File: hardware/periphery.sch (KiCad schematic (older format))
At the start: 32 parts, among them J11 Micro_SD_Card_Ebay, J2 UART0, J8 HR911105_RJ45, Y1 24MHz, Y2 32768

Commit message: Some routing done
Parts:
- removed R37: 2.2, Resistor_SMD:R_0805_2012Metric, symbol Device:R
- removed U? (x2): TLV62568DDC or AP3410/SY8008, Package_TO_SOT_SMD:SOT-23-6, symbol Regulator_Switching:TLV62568DDC
- added C47: 1u, Capacitor_SMD:C_0603_1608Metric, symbol Device:C
- added D1, D2, D3: LED, LED_SMD:LED_0603_1608Metric, symbol Device:LED
- added J1: JAE_SIM_Card_SF72S006, Connector_JAE:JAE_SIM_Card_SF72S006, symbol Connector:JAE_SIM_Card_SF72S006
- added R23: 0R, Resistor_SMD:R_0603_1608Metric, symbol Device:R
- added R26: 10k, Resistor_SMD:R_0603_1608Metric, symbol Device:R
- added R27, R28, R29: 200R, Resistor_SMD:R_0603_1608Metric, symbol Device:R
- C35: value 10u -> 100n; footprint Capacitor_SMD:C_1206_3216Metric -> Capacitor_SMD:C_0603_1608Metric
- J3: renamed from J?; footprint (none) -> Connector_PCBEdge:BUS_PCI_Express_Mini_Full
- gave numbers to parts that had none: 1
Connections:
- net labels added: +1V5, SPI_CS, SPI_MISO, SPI_MOSI, SPI_SCK, USB_H-D+, USB_H-D-, WAKE
- wire segments 85 -> 114
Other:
- moved on the sheet: C33, C34, J3, J8, L1, R14, R15, R18, R19, R20, R21, R30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

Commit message: More routing. CPU power routed. USB li-ion charging added
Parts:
- J3: footprint Connector_PCBEdge:BUS_PCI_Express_Mini_Full -> Connector_PCBEdge:BUS_PCI_Express_Mini_Dual
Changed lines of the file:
@@
 F 0 "J3" H 2700 5900 50  0000 C CNN
 F 1 "Bus_PCI_Express_Mini" H 3250 4750 50  0000 C CNN
-F 2 "Connector_PCBEdge:BUS_PCI_Express_Mini_Full" H 2700 5900 50  0001 C CNN
+F 2 "Connector_PCBEdge:BUS_PCI_Express_Mini_Dual" H 2700 5900 50  0001 C CNN
 F 3 "~" H 2550 4750 50  0001 C CNN
 	1    2700 5900

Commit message: Small touch-ups
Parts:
- removed J2: UART0, Connector_PinSocket_1.27mm:PinSocket_1x04_P1.27mm_Vertical, symbol Connector_Generic:Conn_01x04
- added J2: UART, Connector_PinHeader_2.54mm:PinHeader_1x05_P2.54mm_Vertical, symbol Connector_Generic:Conn_01x05
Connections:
- net +3V3: now also J2.3 (Pin_3)
- net GND: now also J2.4 (Pin_4)
- net UART0_RX: now also J2.1 (Pin_1)
- net UART0_TX: now also J2.2 (Pin_2)
- new net VCC: J2.5 (Pin_5)
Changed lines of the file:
@@
-$EndComp
-$Comp
-L Connector_Generic:Conn_01x04 J2
-U 1 1 5F26BA8E
-P 1350 3200
-F 0 "J2" H 1430 3192 50  0000 L CNN
-F 1 "UART0" H 1430 3101 50  0000 L CNN
-F 2 "Connector_PinSocket_1.27mm:PinSocket_1x04_P1.27mm_Vertical" H 1350 3200 50  0001 C CNN
-F 3 "~" H 1350 3200 50  0001 C CNN
-	1    1350 3200
-	1    0    0    -1
 $EndComp
 $Comp
 L power:GND #PWR0182
 U 1 1 5F270335
-P 1150 3400
-F 0 "#PWR0182" H 1150 3150 50  0001 C CNN
-F 1 "GND" H 1155 3227 50  0001 C CNN
-F 2 "" H 1150 3400 50  0001 C CNN
-F 3 "" H 1150 3400 50  0001 C CNN
-	1    1150 3400
+P 1250 3450
+F 0 "#PWR0182" H 1250 3200 50  0001 C CNN
+F 1 "GND" H 1255 3277 50  0001 C CNN
+F 2 "" H 1250 3450 50  0001 C CNN
+F 3 "" H 1250 3450 50  0001 C CNN
+	1    1250 3450
 	0    1    1    0
 $EndComp
@@
 Text GLabel 1150 5300 0    50   Input ~ 0
 USB-D-
-Text GLabel 1150 3200 0    50   Input ~ 0
+Text GLabel 1250 3250 0    50   Input ~ 0
 UART0_TX
 $Comp
 L power:+3V3 #PWR0181
 U 1 1 5F27004D
-P 1150 3300
-F 0 "#PWR0181" H 1150 3150 50  0001 C CNN
-F 1 "+3V3" V 1150 3500 50  0000 C CNN
-F 2 "" H 1150 3300 50  0001 C CNN
-F 3 "" H 1150 3300 50  0001 C CNN
-	1    1150 3300
+P 1250 3350
+F 0 "#PWR0181" H 1250 3200 50  0001 C CNN
+F 1 "+3V3" V 1250 3550 50  0000 C CNN
+F 2 "" H 1250 3350 50  0001 C CNN
+F 3 "" H 1250 3350 50  0001 C CNN
+	1    1250 3350
 	0    -1   -1   0
 $EndComp
-Text GLabel 1150 3100 0    50   Input ~ 0
+Text GLabel 1250 3150 0    50   Input ~ 0
 UART0_RX
 $Comp
@@
 Text Label 1600 5300 0    50   ~ 0
 USB_H-D-
+$Comp
+L power:VCC #PWR0176
+U 1 1 62786CAF
+P 1250 3550
+F 0 "#PWR0176" H 1250 3400 50  0001 C CNN
+F 1 "VCC" V 1265 3677 50  0000 L CNN
+F 2 "" H 1250 3550 50  0001 C CNN
+F 3 "" H 1250 3550 50  0001 C CNN
+	1    1250 3550
+	0    -1   -1   0
+$EndComp
+$Comp
+L Connector_Generic:Conn_01x05 J2
+U 1 1 6279ABFA
+P 1450 3350
+F 0 "J2" H 1530 3392 50  0000 L CNN
+F 1 "UART" H 1530 3301 50  0000 L CNN
+F 2 "Connector_PinHeader_2.54mm:PinHeader_1x05_P2.54mm_Vertical" H 1450 3350 50  0001 C CNN
+F 3 "~" H 1450 3350 50  0001 C CNN
+	1    1450 3350
+	1    0    0    -1
+$EndComp
 $EndSCHEMATC

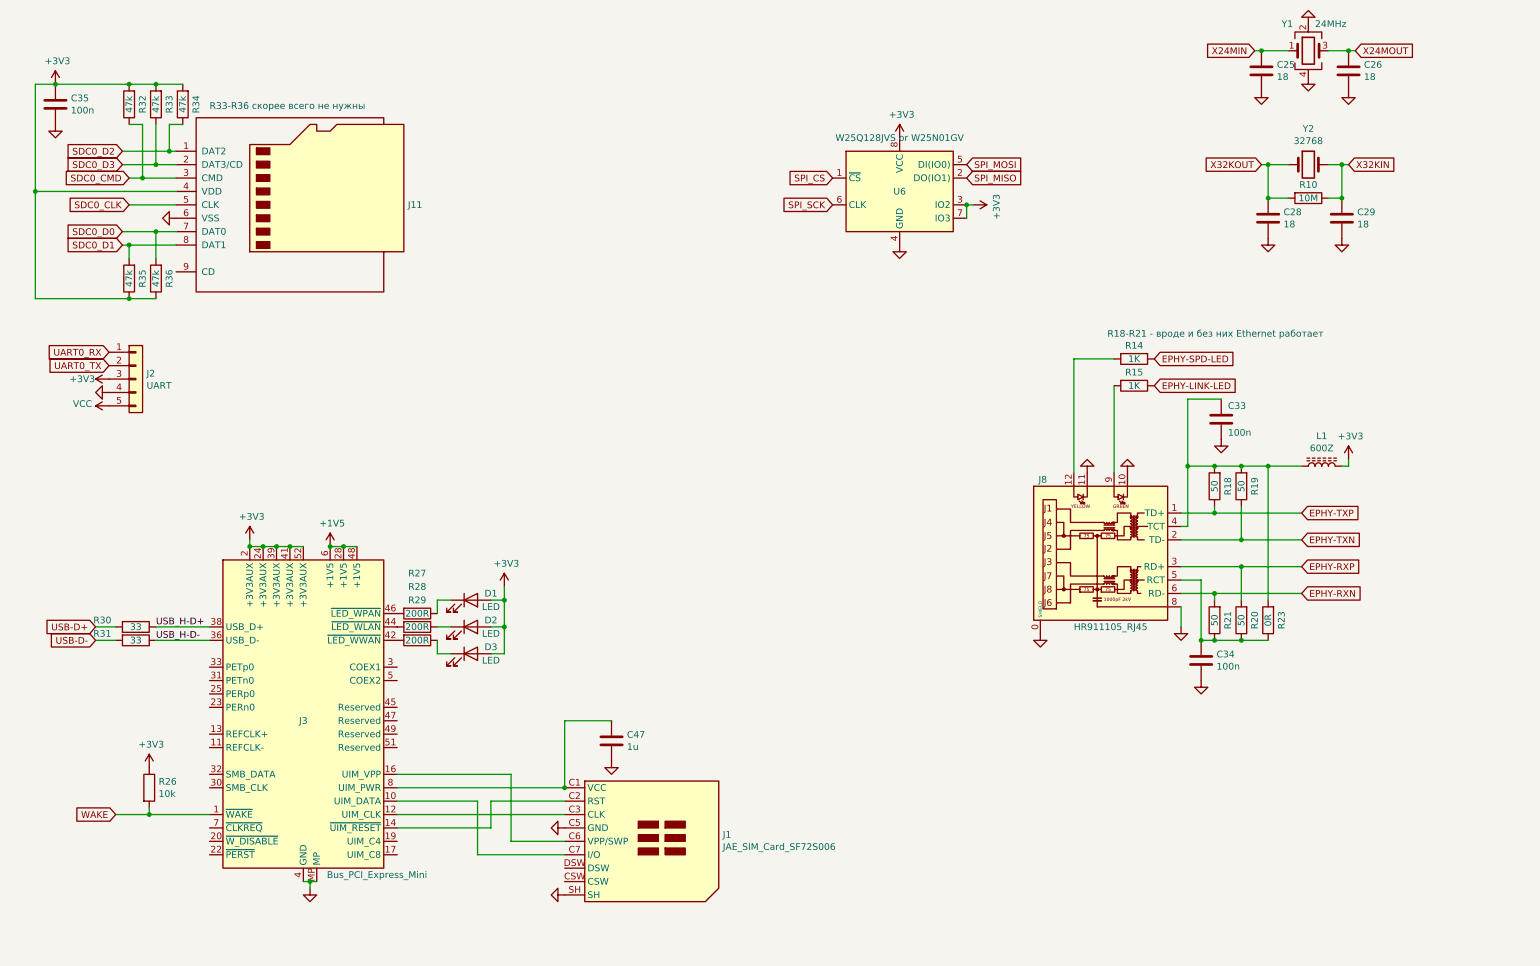
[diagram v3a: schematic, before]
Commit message: Added USB UART
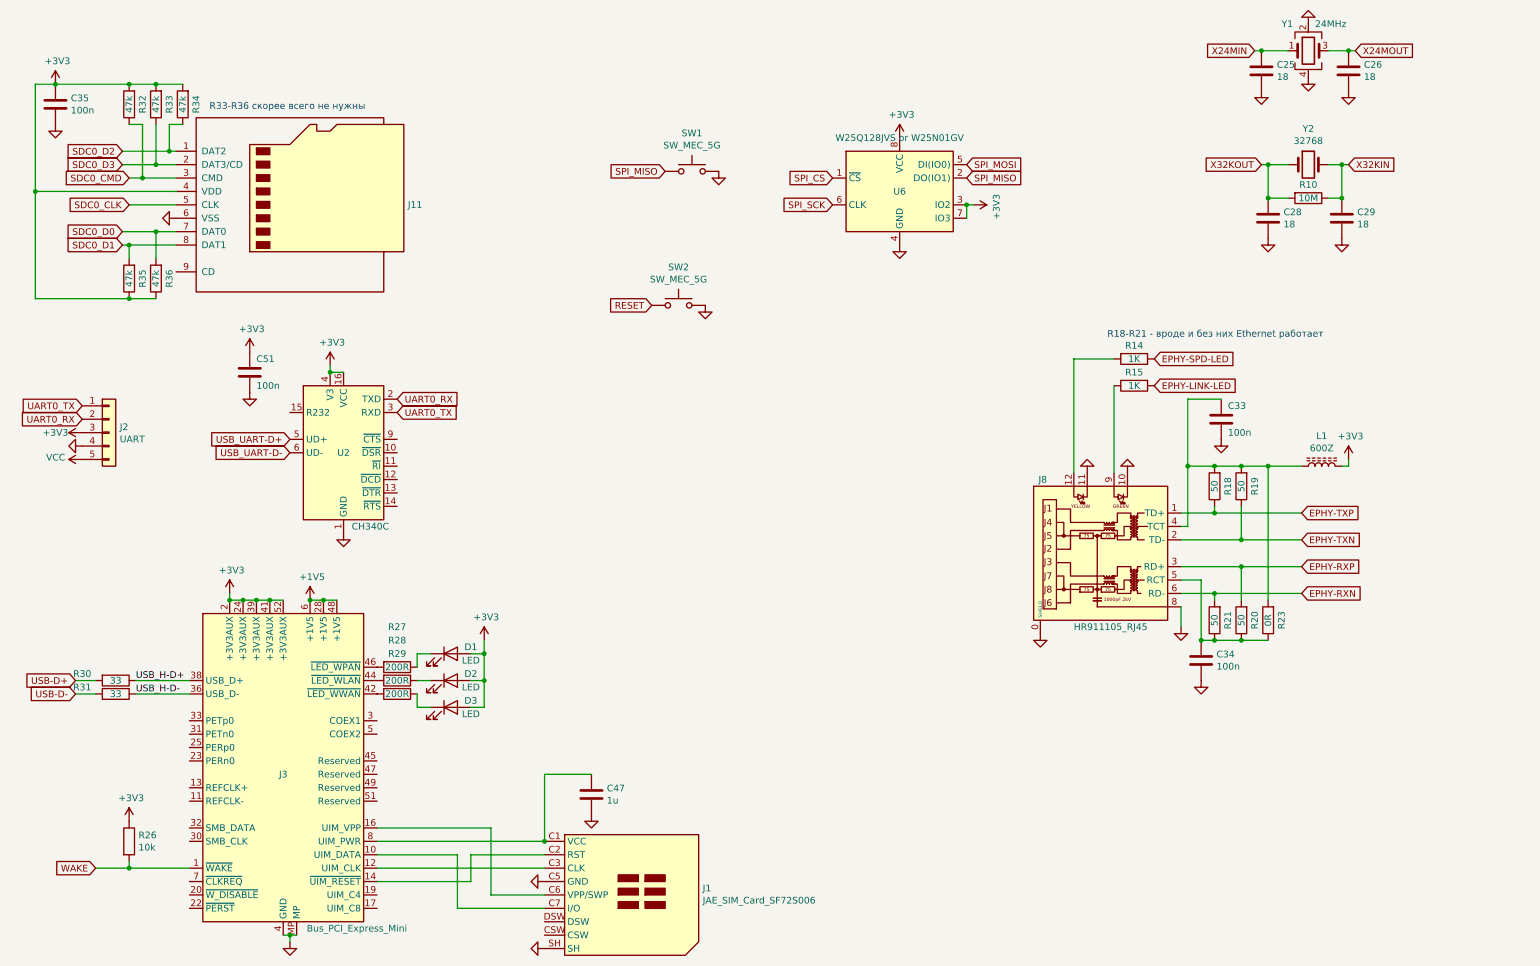
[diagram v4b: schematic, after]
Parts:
- added C51: 100n, Capacitor_SMD:C_0603_1608Metric, symbol Device:C
- added SW1, SW2: SW_MEC_5G, Button_Switch_SMD:SW_SPST_Omron_B3FS-100xP, symbol Switch:SW_MEC_5G
- added U2: CH340C, Package_SO:SOIC-16_3.9x9.9mm_P1.27mm, symbol Interface_USB:CH340C
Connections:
- net +3V3: now also C51.1, U2.16 (VCC), U2.4 (V3)
- net GND: now also C51.2, SW1.3 (B), SW1.4 (B), SW2.3 (B), SW2.4 (B), U2.1 (GND)
- net SPI_MISO: now also SW1.1 (A), SW1.2 (A)
- net UART0_RX: now also J2.2 (Pin_2), U2.2 (TXD); no longer J2.1 (Pin_1)
- net UART0_TX: now also J2.1 (Pin_1), U2.3 (RXD); no longer J2.2 (Pin_2)
- new net RESET: SW2.1 (A), SW2.2 (A)
- new net USB_UART-D+: U2.5 (UD+)
- new net USB_UART-D-: U2.6 (UD-)
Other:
- moved on the sheet: C47, D1, D2, D3, J1, J2, J3, R26, R27, R28, R29, R30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

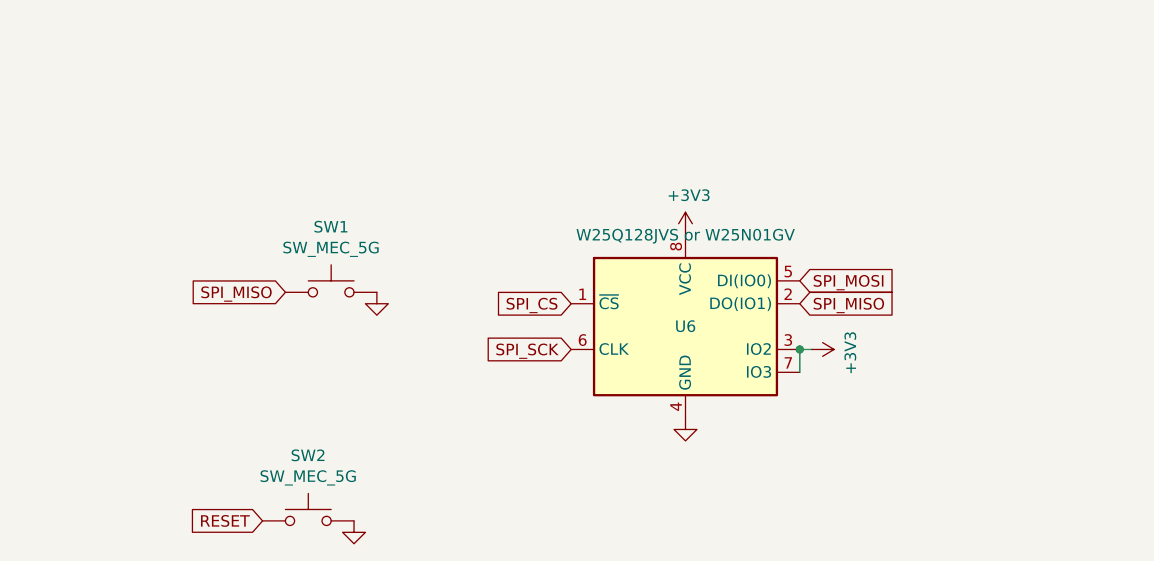
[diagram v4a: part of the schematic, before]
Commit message: Removed FEL button
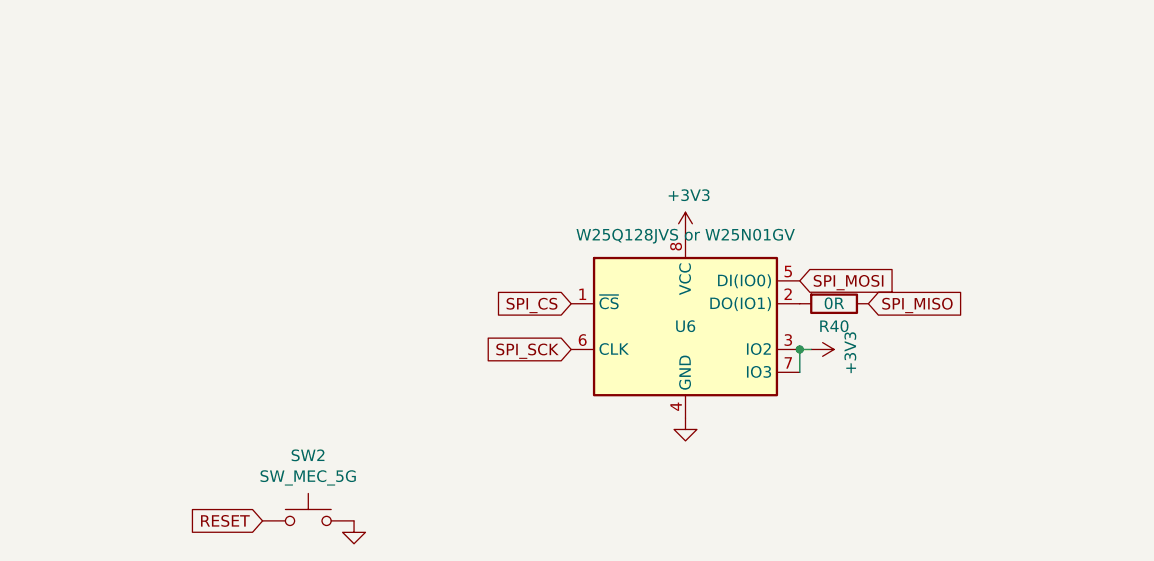
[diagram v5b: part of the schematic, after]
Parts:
- removed SW1: SW_MEC_5G, Button_Switch_SMD:SW_SPST_Omron_B3FS-100xP, symbol Switch:SW_MEC_5G
- added R40: 0R, Resistor_SMD:R_0603_1608Metric, symbol Device:R
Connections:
- net SPI_MISO: now also R40.1; no longer U6.2 (DO(IO1))
- new net: R40.2, U6.2 (DO(IO1))
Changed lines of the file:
@@
 Text GLabel 6650 2050 0    50   Input ~ 0
 SPI_SCK
-Text GLabel 7650 1850 2    50   Input ~ 0
+Text GLabel 7950 1850 2    50   Input ~ 0
 SPI_MISO
 Text GLabel 7650 1750 2    50   Input ~ 0
@@
 UART0_RX
 $Comp
-L Switch:SW_MEC_5G SW1
-U 1 1 62909E2A
-P 5600 1800
-F 0 "SW1" H 5600 2085 50  0000 C CNN
-F 1 "SW_MEC_5G" H 5600 1994 50  0000 C CNN
-F 2 "Button_Switch_SMD:SW_SPST_Omron_B3FS-100xP" H 5600 2000 50  0001 C CNN
-F 3 "http://www.apem.com/int/index.php?controller=attachment&id_attachment=488" H 5600 2000 50  0001 C CNN
-	1    5600 1800
-	1    0    0    -1
-$EndComp
-$Comp
-L power:GND #PWR0177
-U 1 1 6290BF0D
-P 5800 1800
-F 0 "#PWR0177" H 5800 1550 50  0001 C CNN
-F 1 "GND" H 5805 1627 50  0001 C CNN
-F 2 "" H 5800 1800 50  0001 C CNN
-F 3 "" H 5800 1800 50  0001 C CNN
-	1    5800 1800
-	1    0    0    -1
-$EndComp
-$Comp
 L Switch:SW_MEC_5G SW2
 U 1 1 62914EBE
@@
 Text GLabel 5300 2800 0    50   Input ~ 0
 RESET
-Text GLabel 5400 1800 0    50   Input ~ 0
-SPI_MISO
+$Comp
+L Device:R R40
+U 1 1 629C3A1F
+P 7800 1850
+F 0 "R40" V 7900 1850 50  0000 C CNN
+F 1 "0R" V 7800 1850 50  0000 C CNN
+F 2 "Resistor_SMD:R_0603_1608Metric" V 7730 1850 50  0001 C CNN
+F 3 "~" H 7800 1850 50  0001 C CNN
+	1    7800 1850
+	0    1    1    0
+$EndComp
 $EndSCHEMATC

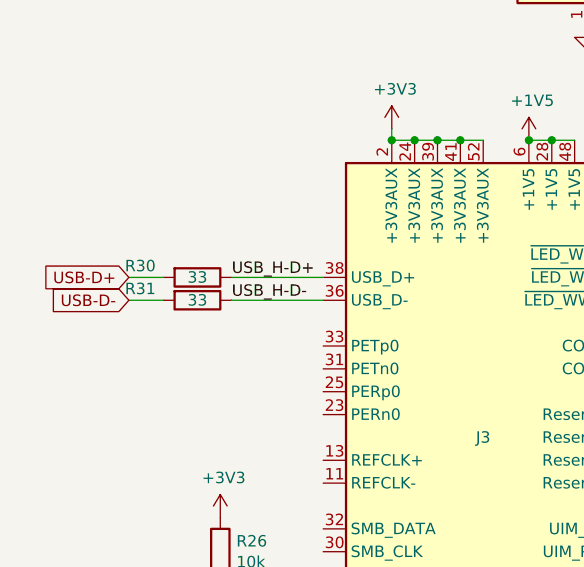
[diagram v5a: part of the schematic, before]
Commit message: Removed USB series resistors on mPCIe side
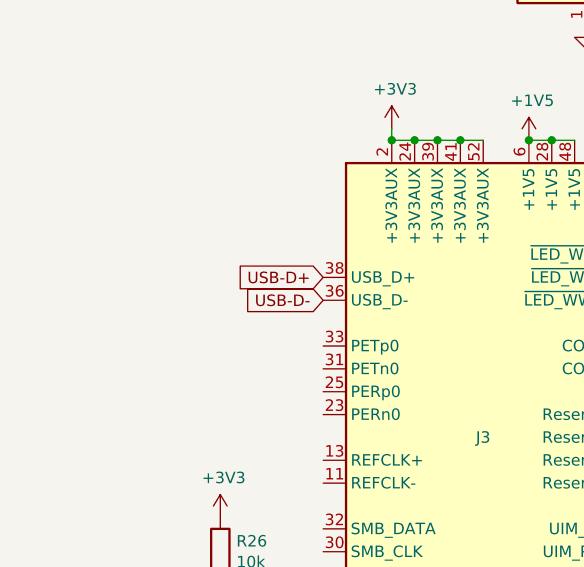
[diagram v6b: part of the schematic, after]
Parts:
- removed R30, R31: 33, Resistor_SMD:R_0603_1608Metric, symbol Device:R
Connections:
- net USB_H-D+ is gone; now on net USB-D+: J3.38 (USB_D+)
- net USB_H-D- is gone; now on net USB-D-: J3.36 (USB_D-)
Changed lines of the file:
@@
 	0    1    1    0
 $EndComp
-Text GLabel 1000 5600 0    50   Input ~ 0
+Text GLabel 1850 5600 0    50   Input ~ 0
 USB-D+
-Text GLabel 1000 5700 0    50   Input ~ 0
+Text GLabel 1850 5700 0    50   Input ~ 0
 USB-D-
 Text GLabel 3400 3600 2    50   Input ~ 0
@@
 Text GLabel 3400 3500 2    50   Input ~ 0
 UART0_RX
-$Comp
-L Device:R R30
-U 1 1 5FE10647
-P 1300 5600
-F 0 "R30" V 1250 5350 50  0000 C CNN
-F 1 "33" V 1300 5600 50  0000 C CNN
-F 2 "Resistor_SMD:R_0603_1608Metric" V 1230 5600 50  0001 C CNN
-F 3 "~" H 1300 5600 50  0001 C CNN
-	1    1300 5600
-	0    1    1    0
-$EndComp
-$Comp
-L Device:R R31
-U 1 1 5FE10E92
-P 1300 5700
-F 0 "R31" V 1250 5450 50  0000 C CNN
-F 1 "33" V 1300 5700 50  0000 C CNN
-F 2 "Resistor_SMD:R_0603_1608Metric" V 1230 5700 50  0001 C CNN
-F 3 "~" H 1300 5700 50  0001 C CNN
-	1    1300 5700
-	0    1    1    0
-$EndComp
-Wire Wire Line
-	1150 5600 1000 5600
-Wire Wire Line
-	1150 5700 1000 5700
 Text Notes 8700 3050 0    50   ~ 0
 R18-R21 - вроде и без них Ethernet работает
@@
 Wire Wire Line
 	1400 7000 1850 7000
-Wire Wire Line
-	1450 5600 1850 5600
-Wire Wire Line
-	1450 5700 1850 5700
-Text Label 1450 5600 0    50   ~ 0
-USB_H-D+
-Text Label 1450 5700 0    50   ~ 0
-USB_H-D-
 $Comp
 L power:VCC #PWR0176

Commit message: Added an "RDY" LED
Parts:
- added D5: LED, LED_SMD:LED_0603_1608Metric, symbol Device:LED
- added R31: 200R, Resistor_SMD:R_0603_1608Metric, symbol Device:R
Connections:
- net +3V3: now also D5.2 (A)
- new net: D5.1 (K), R31.1
- new net SDC1_D2: R31.2
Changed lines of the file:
@@
 	0    1    1    0
 $EndComp
+$Comp
+L Device:LED D5
+U 1 1 6228B327
+P 5300 4950
+F 0 "D5" H 5450 5000 50  0000 C CNN
+F 1 "LED" H 5450 4900 50  0000 C CNN
+F 2 "LED_SMD:LED_0603_1608Metric" H 5300 4950 50  0001 C CNN
+F 3 "~" H 5300 4950 50  0001 C CNN
+	1    5300 4950
+	1    0    0    -1
+$EndComp
+$Comp
+L Device:R R31
+U 1 1 6228BB22
+P 5000 4950
+F 0 "R31" V 4900 4950 50  0000 C CNN
+F 1 "200R" V 5000 4950 50  0000 C CNN
+F 2 "Resistor_SMD:R_0603_1608Metric" V 4930 4950 50  0001 C CNN
+F 3 "~" H 5000 4950 50  0001 C CNN
+	1    5000 4950
+	0    1    1    0
+$EndComp
+$Comp
+L power:+3V3 #PWR030
+U 1 1 6228C3F8
+P 5450 4800
+F 0 "#PWR030" H 5450 4650 50  0001 C CNN
+F 1 "+3V3" H 5465 4973 50  0000 C CNN
+F 2 "" H 5450 4800 50  0001 C CNN
+F 3 "" H 5450 4800 50  0001 C CNN
+	1    5450 4800
+	1    0    0    -1
+$EndComp
+Wire Wire Line
+	5450 4800 5450 4950
+Text GLabel 4850 4950 0    50   Input ~ 0
+SDC1_D2
 $EndSCHEMATC

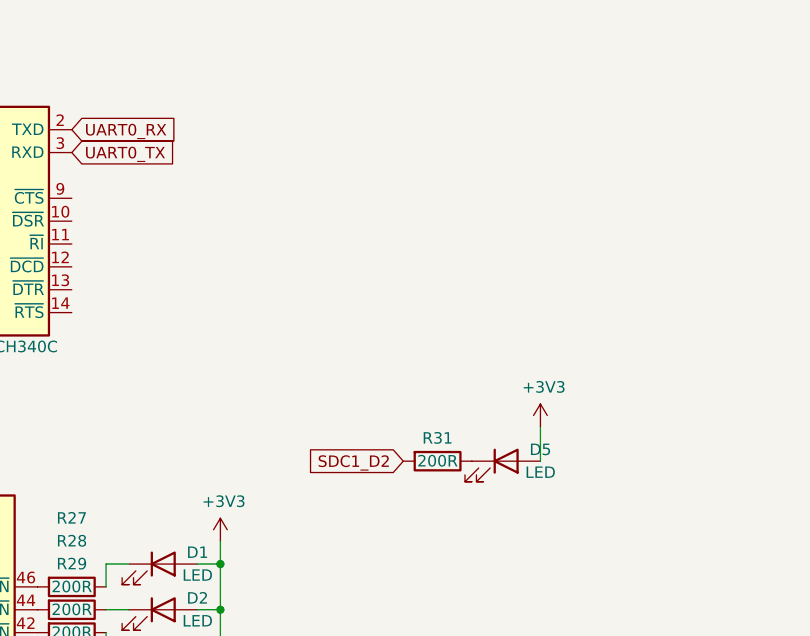
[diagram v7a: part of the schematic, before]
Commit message: Added 0R for USB_ID pin + Moved OK LED to licheePi default GPIO
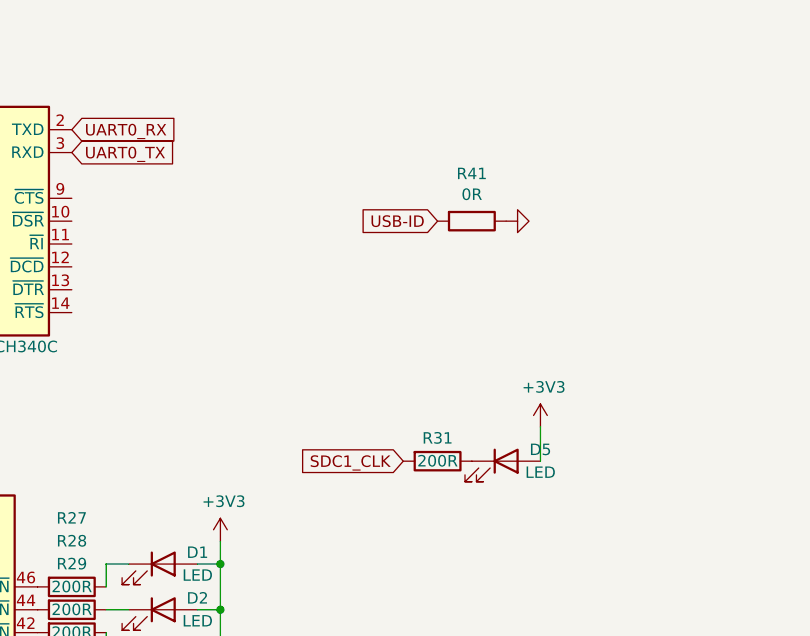
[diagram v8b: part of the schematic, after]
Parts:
- added R41: 0R, Resistor_SMD:R_0603_1608Metric, symbol Device:R
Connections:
- net GND: now also R41.1
- net SDC1_D2 renamed SDC1_CLK
- new net USB-ID: R41.2
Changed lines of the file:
@@
 Wire Wire Line
 	5450 4800 5450 4950
+Text GLabel 5000 3900 0    50   Input ~ 0
+USB-ID
+$Comp
+L Device:R R41
+U 1 1 62382756
+P 5150 3900
+F 0 "R41" V 4943 3900 50  0000 C CNN
+F 1 "0R" V 5034 3900 50  0000 C CNN
+F 2 "Resistor_SMD:R_0603_1608Metric" V 5080 3900 50  0001 C CNN
+F 3 "~" H 5150 3900 50  0001 C CNN
+	1    5150 3900
+	0    1    1    0
+$EndComp
+$Comp
+L power:GND #PWR07
+U 1 1 623865EE
+P 5300 3900
+F 0 "#PWR07" H 5300 3650 50  0001 C CNN
+F 1 "GND" H 5305 3727 50  0001 C CNN
+F 2 "" H 5300 3900 50  0001 C CNN
+F 3 "" H 5300 3900 50  0001 C CNN
+	1    5300 3900
+	0    -1   -1   0
+$EndComp
 Text GLabel 4850 4950 0    50   Input ~ 0
-SDC1_D2
+SDC1_CLK
 $EndSCHEMATC
